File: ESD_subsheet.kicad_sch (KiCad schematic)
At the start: 12 parts

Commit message: starter PCB
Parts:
- renumbered D4 to D25, D8 to D26, D15 to D27, D11 to D28, D16 to D29, D12 to D30, R3 to R27, R4 to R28, R15 to R29, R8 to R30, R18 to R31, R14 to R32
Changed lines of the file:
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@@
 		(on_board yes)
 		(dnp no)
-		(property "Reference" "#PWR010"
+		(property "Reference" "#PWR062"
 			(at 194.31 57.15 0)
 			(effects
@@
 			(project "PCB_Schematic"
 				(path "/a0c17764-e0d1-4df5-b871-1489cf266494/bd8fac2e-3f10-4282-9936-a5d1cb93bf65"
-					(reference "#PWR010")
+					(reference "#PWR062")
 					(unit 1)
 				)
@@
 		(dnp no)
 		(fields_autoplaced yes)
-		(property "Reference" "#PWR011"
+		(property "Reference" "#PWR064"
 			(at 245.11 57.15 0)
 			(effects
@@
 			(project "PCB_Schematic"
 				(path "/a0c17764-e0d1-4df5-b871-1489cf266494/bd8fac2e-3f10-4282-9936-a5d1cb93bf65"
-					(reference "#PWR011")
+					(reference "#PWR064")
 					(unit 1)
 				)
@@
 		(on_board yes)
 		(dnp no)
-		(property "Reference" "R4"
+		(property "Reference" "R28"
 			(at 53.34 134.62 90)
 			(effects
@@
 			(project "PCB_Schematic"
 				(path "/a0c17764-e0d1-4df5-b871-1489cf266494/bd8fac2e-3f10-4282-9936-a5d1cb93bf65"
-					(reference "R4")
+					(reference "R28")
 					(unit 1)
 				)
@@
 		(on_board yes)
 		(dnp no)
-		(property "Reference" "D11"
+		(property "Reference" "D28"
 			(at 198.12 74.9299 90)
 			(effects
@@
 			(project "PCB_Schematic"
 				(path "/a0c17764-e0d1-4df5-b871-1489cf266494/bd8fac2e-3f10-4282-9936-a5d1cb93bf65"
-					(reference "D11")
+					(reference "D28")
 					(unit 1)
 				)
@@
 		(dnp no)
 		(fields_autoplaced yes)
-		(property "Reference" "D4"
+		(property "Reference" "D25"
 			(at 62.23 109.2199 90)
 			(effects
@@
 			(project "PCB_Schematic"
 				(path "/a0c17764-e0d1-4df5-b871-1489cf266494/bd8fac2e-3f10-4282-9936-a5d1cb93bf65"
-					(reference "D4")
+					(reference "D25")
 					(unit 1)
 				)
@@
 		(on_board yes)
 		(dnp no)
-		(property "Reference" "D8"
+		(property "Reference" "D26"
 			(at 63.5 142.24 90)
 			(effects
@@
 			(project "PCB_Schematic"
 				(path "/a0c17764-e0d1-4df5-b871-1489cf266494/bd8fac2e-3f10-4282-9936-a5d1cb93bf65"
-					(reference "D8")
+					(reference "D26")
 					(unit 1)
 				)
@@
 		(on_board yes)
 		(dnp no)
-		(property "Reference" "R14"
+		(property "Reference" "R32"
 			(at 238.76 67.31 90)
 			(effects
@@
 			(project "PCB_Schematic"
 				(path "/a0c17764-e0d1-4df5-b871-1489cf266494/bd8fac2e-3f10-4282-9936-a5d1cb93bf65"
-					(reference "R14")
+					(reference "R32")
 					(unit 1)
 				)
@@
 		(dnp no)
 		(fields_autoplaced yes)
-		(property "Reference" "#PWR08"
+		(property "Reference" "#PWR065"
 			(at 246.38 86.36 0)
 			(effects
@@
 			(project "PCB_Schematic"
 				(path "/a0c17764-e0d1-4df5-b871-1489cf266494/bd8fac2e-3f10-4282-9936-a5d1cb93bf65"
-					(reference "#PWR08")
+					(reference "#PWR065")
 					(unit 1)
 				)
@@
 		(on_board yes)
 		(dnp no)
-		(property "Reference" "R18"
+		(property "Reference" "R31"
 			(at 237.49 38.1 90)
 			(effects
@@
 			(project "PCB_Schematic"
 				(path "/a0c17764-e0d1-4df5-b871-1489cf266494/bd8fac2e-3f10-4282-9936-a5d1cb93bf65"
-					(reference "R18")
+					(reference "R31")
 					(unit 1)
 				)
@@
 		(dnp no)
 		(fields_autoplaced yes)
-		(property "Reference" "D16"
+		(property "Reference" "D29"
 			(at 247.65 45.7199 90)
 			(effects
@@
 			(project "PCB_Schematic"
 				(path "/a0c17764-e0d1-4df5-b871-1489cf266494/bd8fac2e-3f10-4282-9936-a5d1cb93bf65"
-					(reference "D16")
+					(reference "D29")
 					(unit 1)
 				)
@@
 		(dnp no)
 		(fields_autoplaced yes)
-		(property "Reference" "#PWR03"
+		(property "Reference" "#PWR060"
 			(at 59.69 120.65 0)
 			(effects
@@
 			(project "PCB_Schematic"
 				(path "/a0c17764-e0d1-4df5-b871-1489cf266494/bd8fac2e-3f10-4282-9936-a5d1cb93bf65"
-					(reference "#PWR03")
+					(reference "#PWR060")
 					(unit 1)
 				)
@@
 		(dnp no)
 		(fields_autoplaced yes)
-		(property "Reference" "D12"
+		(property "Reference" "D30"
 			(at 248.92 74.9299 90)
 			(effects
@@
 			(project "PCB_Schematic"
 				(path "/a0c17764-e0d1-4df5-b871-1489cf266494/bd8fac2e-3f10-4282-9936-a5d1cb93bf65"
-					(reference "D12")
+					(reference "D30")
 					(unit 1)
 				)
@@
 		(dnp no)
 		(fields_autoplaced yes)
-		(property "Reference" "#PWR04"
+		(property "Reference" "#PWR061"
 			(at 60.96 153.67 0)
 			(effects
@@
 			(project "PCB_Schematic"
 				(path "/a0c17764-e0d1-4df5-b871-1489cf266494/bd8fac2e-3f10-4282-9936-a5d1cb93bf65"
-					(reference "#PWR04")
+					(reference "#PWR061")
 					(unit 1)
 				)
@@
 		(dnp no)
 		(fields_autoplaced yes)
-		(property "Reference" "#PWR07"
+		(property "Reference" "#PWR063"
 			(at 195.58 86.36 0)
 			(effects
@@
 			(project "PCB_Schematic"
 				(path "/a0c17764-e0d1-4df5-b871-1489cf266494/bd8fac2e-3f10-4282-9936-a5d1cb93bf65"
-					(reference "#PWR07")
+					(reference "#PWR063")
 					(unit 1)
 				)
@@
 		(on_board yes)
 		(dnp no)
-		(property "Reference" "R15"
+		(property "Reference" "R29"
 			(at 186.69 38.1 90)
 			(effects
@@
 			(project "PCB_Schematic"
 				(path "/a0c17764-e0d1-4df5-b871-1489cf266494/bd8fac2e-3f10-4282-9936-a5d1cb93bf65"
-					(reference "R15")
+					(reference "R29")
 					(unit 1)
 				)
@@
 		(dnp no)
 		(fields_autoplaced yes)
-		(property "Reference" "D15"
+		(property "Reference" "D27"
 			(at 196.85 45.7199 90)
 			(effects
@@
 			(project "PCB_Schematic"
 				(path "/a0c17764-e0d1-4df5-b871-1489cf266494/bd8fac2e-3f10-4282-9936-a5d1cb93bf65"
-					(reference "D15")
+					(reference "D27")
 					(unit 1)
 				)
@@
 		(on_board yes)
 		(dnp no)
-		(property "Reference" "R8"
+		(property "Reference" "R30"
 			(at 187.96 67.31 90)
 			(effects
@@
 			(project "PCB_Schematic"
 				(path "/a0c17764-e0d1-4df5-b871-1489cf266494/bd8fac2e-3f10-4282-9936-a5d1cb93bf65"
-					(reference "R8")
+					(reference "R30")
 					(unit 1)
 				)
@@
 		(on_board yes)
 		(dnp no)
-		(property "Reference" "R3"
+		(property "Reference" "R27"
 			(at 52.07 101.6 90)
 			(effects
@@
 			(project "PCB_Schematic"
 				(path "/a0c17764-e0d1-4df5-b871-1489cf266494/bd8fac2e-3f10-4282-9936-a5d1cb93bf65"
-					(reference "R3")
-					(unit 1)
-				)
+					(reference "R27")
+					(unit 1)
+				)

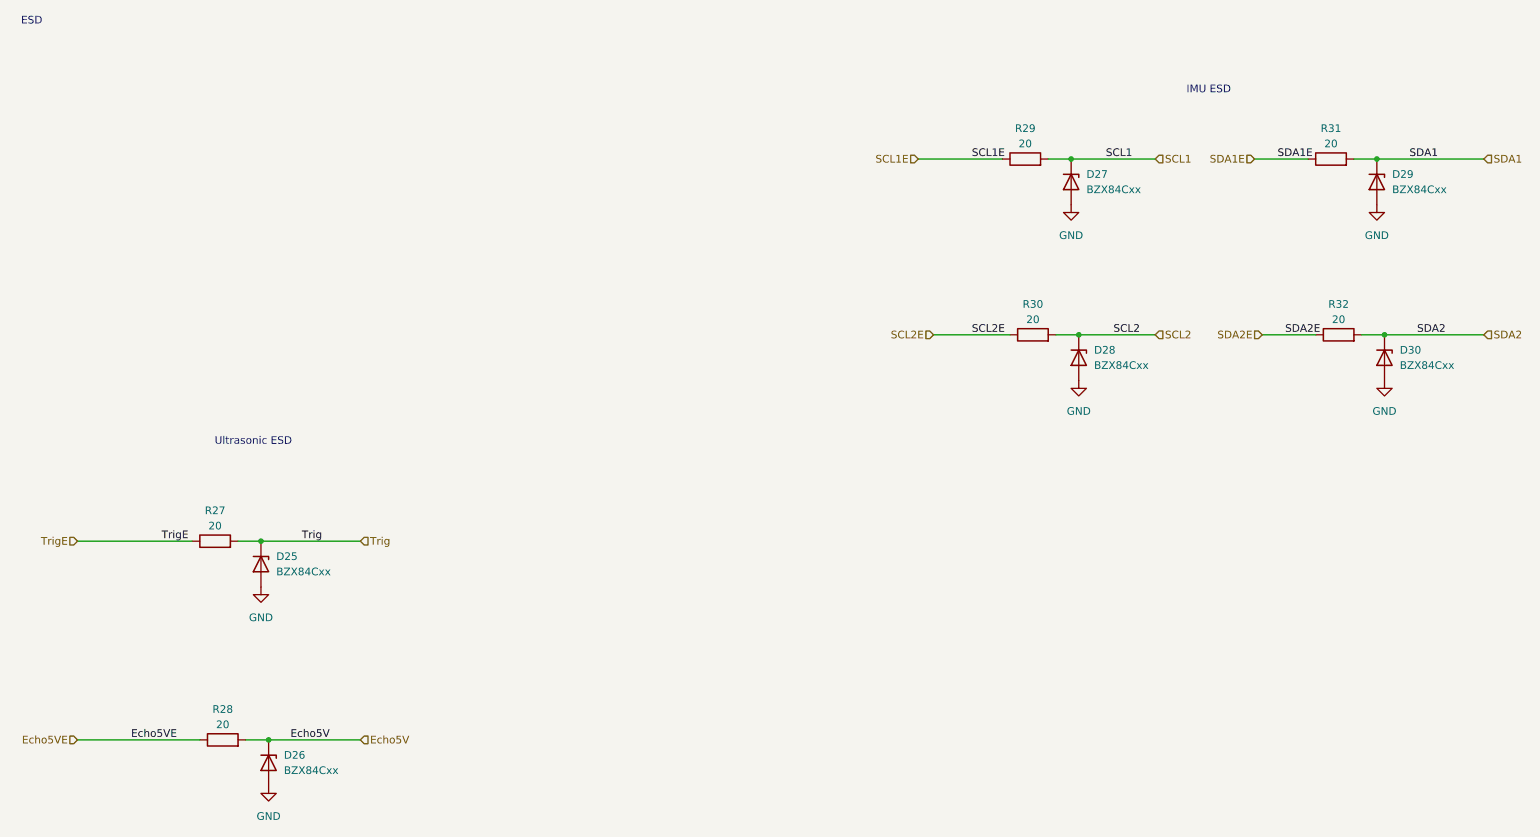
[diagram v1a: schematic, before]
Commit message: added testpoints to schematic for important sigs
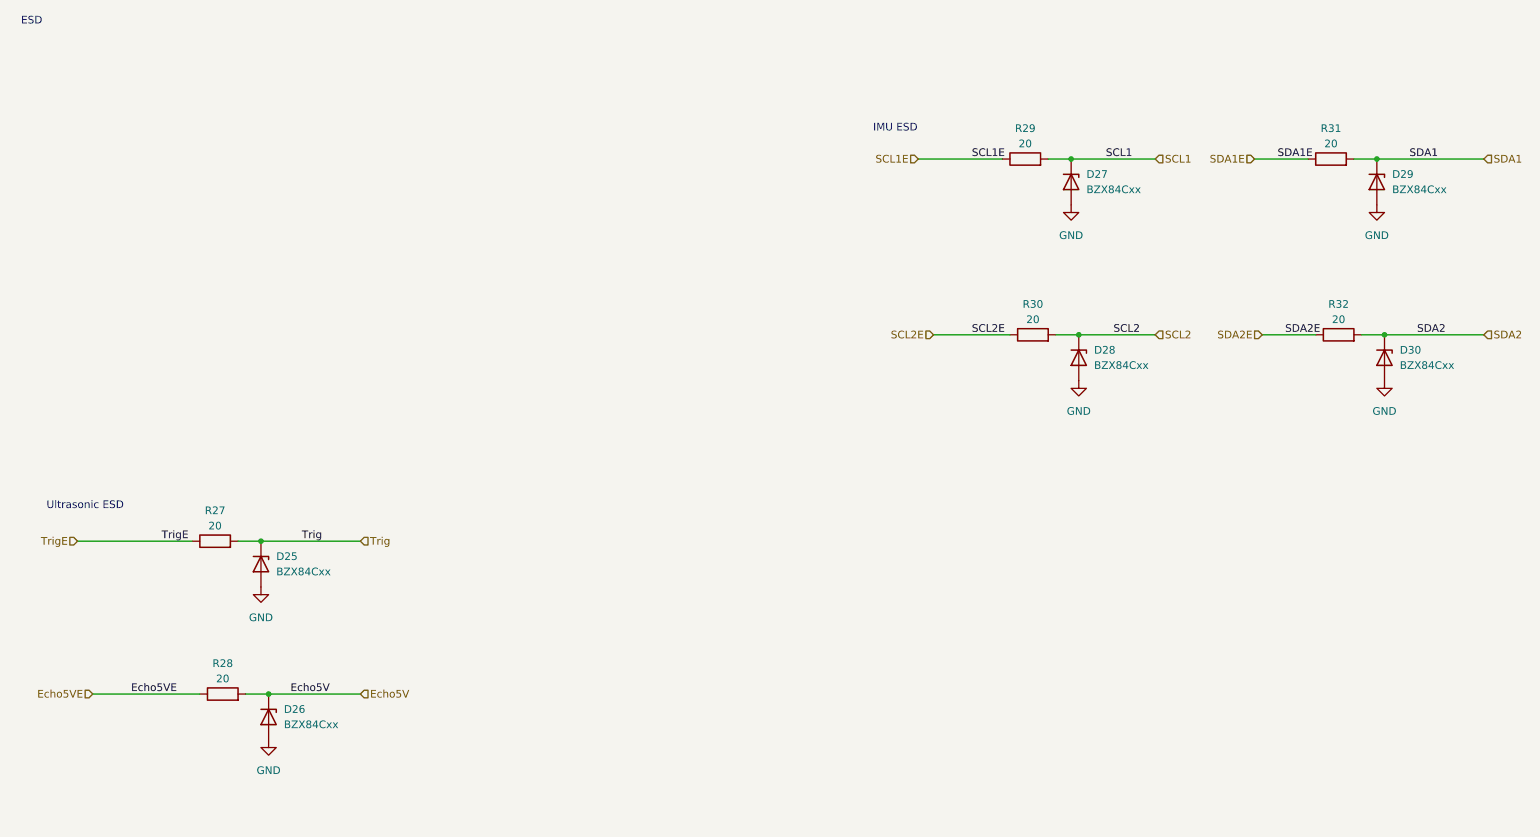
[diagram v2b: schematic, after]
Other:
- moved on the sheet: D26, R28

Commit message: footprint
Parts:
- renumbered D25 to D15, D26 to D16, D27 to D17, D28 to D18, D29 to D19, D30 to D20, R27 to R21, R28 to R22, R29 to R23, R30 to R24, R31 to R25, R32 to R26
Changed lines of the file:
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@@
 		(on_board yes)
 		(dnp no)
-		(property "Reference" "R28"
+		(property "Reference" "R22"
 			(at 53.34 127 90)
 			(effects
@@
 			(project "PCB_Schematic"
 				(path "/a0c17764-e0d1-4df5-b871-1489cf266494/bd8fac2e-3f10-4282-9936-a5d1cb93bf65"
-					(reference "R28")
+					(reference "R22")
 					(unit 1)
 				)
@@
 		(on_board yes)
 		(dnp no)
-		(property "Reference" "D28"
+		(property "Reference" "D18"
 			(at 198.12 74.9299 90)
 			(effects
@@
 			(project "PCB_Schematic"
 				(path "/a0c17764-e0d1-4df5-b871-1489cf266494/bd8fac2e-3f10-4282-9936-a5d1cb93bf65"
-					(reference "D28")
+					(reference "D18")
 					(unit 1)
 				)
@@
 		(dnp no)
 		(fields_autoplaced yes)
-		(property "Reference" "D25"
+		(property "Reference" "D15"
 			(at 62.23 109.2199 90)
 			(effects
@@
 			(project "PCB_Schematic"
 				(path "/a0c17764-e0d1-4df5-b871-1489cf266494/bd8fac2e-3f10-4282-9936-a5d1cb93bf65"
-					(reference "D25")
+					(reference "D15")
 					(unit 1)
 				)
@@
 		(on_board yes)
 		(dnp no)
-		(property "Reference" "D26"
+		(property "Reference" "D16"
 			(at 63.5 134.62 90)
 			(effects
@@
 			(project "PCB_Schematic"
 				(path "/a0c17764-e0d1-4df5-b871-1489cf266494/bd8fac2e-3f10-4282-9936-a5d1cb93bf65"
-					(reference "D26")
+					(reference "D16")
 					(unit 1)
 				)
@@
 		(on_board yes)
 		(dnp no)
-		(property "Reference" "R32"
+		(property "Reference" "R26"
 			(at 238.76 67.31 90)
 			(effects
@@
 			(project "PCB_Schematic"
 				(path "/a0c17764-e0d1-4df5-b871-1489cf266494/bd8fac2e-3f10-4282-9936-a5d1cb93bf65"
-					(reference "R32")
+					(reference "R26")
 					(unit 1)
 				)
@@
 		(on_board yes)
 		(dnp no)
-		(property "Reference" "R31"
+		(property "Reference" "R25"
 			(at 237.49 38.1 90)
 			(effects
@@
 			(project "PCB_Schematic"
 				(path "/a0c17764-e0d1-4df5-b871-1489cf266494/bd8fac2e-3f10-4282-9936-a5d1cb93bf65"
-					(reference "R31")
+					(reference "R25")
 					(unit 1)
 				)
@@
 		(dnp no)
 		(fields_autoplaced yes)
-		(property "Reference" "D29"
+		(property "Reference" "D19"
 			(at 247.65 45.7199 90)
 			(effects
@@
 			(project "PCB_Schematic"
 				(path "/a0c17764-e0d1-4df5-b871-1489cf266494/bd8fac2e-3f10-4282-9936-a5d1cb93bf65"
-					(reference "D29")
+					(reference "D19")
 					(unit 1)
 				)
@@
 		(dnp no)
 		(fields_autoplaced yes)
-		(property "Reference" "D30"
+		(property "Reference" "D20"
 			(at 248.92 74.9299 90)
 			(effects
@@
 			(project "PCB_Schematic"
 				(path "/a0c17764-e0d1-4df5-b871-1489cf266494/bd8fac2e-3f10-4282-9936-a5d1cb93bf65"
-					(reference "D30")
+					(reference "D20")
 					(unit 1)
 				)
@@
 		(on_board yes)
 		(dnp no)
-		(property "Reference" "R29"
+		(property "Reference" "R23"
 			(at 186.69 38.1 90)
 			(effects
@@
 			(project "PCB_Schematic"
 				(path "/a0c17764-e0d1-4df5-b871-1489cf266494/bd8fac2e-3f10-4282-9936-a5d1cb93bf65"
-					(reference "R29")
+					(reference "R23")
 					(unit 1)
 				)
@@
 		(dnp no)
 		(fields_autoplaced yes)
-		(property "Reference" "D27"
+		(property "Reference" "D17"
 			(at 196.85 45.7199 90)
 			(effects
@@
 			(project "PCB_Schematic"
 				(path "/a0c17764-e0d1-4df5-b871-1489cf266494/bd8fac2e-3f10-4282-9936-a5d1cb93bf65"
-					(reference "D27")
+					(reference "D17")
 					(unit 1)
 				)
@@
 		(on_board yes)
 		(dnp no)
-		(property "Reference" "R30"
+		(property "Reference" "R24"
 			(at 187.96 67.31 90)
 			(effects
@@
 			(project "PCB_Schematic"
 				(path "/a0c17764-e0d1-4df5-b871-1489cf266494/bd8fac2e-3f10-4282-9936-a5d1cb93bf65"
-					(reference "R30")
+					(reference "R24")
 					(unit 1)
 				)
@@
 		(on_board yes)
 		(dnp no)
-		(property "Reference" "R27"
+		(property "Reference" "R21"
 			(at 52.07 101.6 90)
 			(effects
@@
 			(project "PCB_Schematic"
 				(path "/a0c17764-e0d1-4df5-b871-1489cf266494/bd8fac2e-3f10-4282-9936-a5d1cb93bf65"
-					(reference "R27")
-					(unit 1)
-				)
+					(reference "R21")
+					(unit 1)
+				)
